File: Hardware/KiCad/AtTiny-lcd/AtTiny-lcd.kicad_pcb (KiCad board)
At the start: 2 copper layers, 7 parts, among them J1 Conn_01x04_Pin, J2 Conn_01x04_Pin, Q1 BC817, U1 ATtiny414-SS

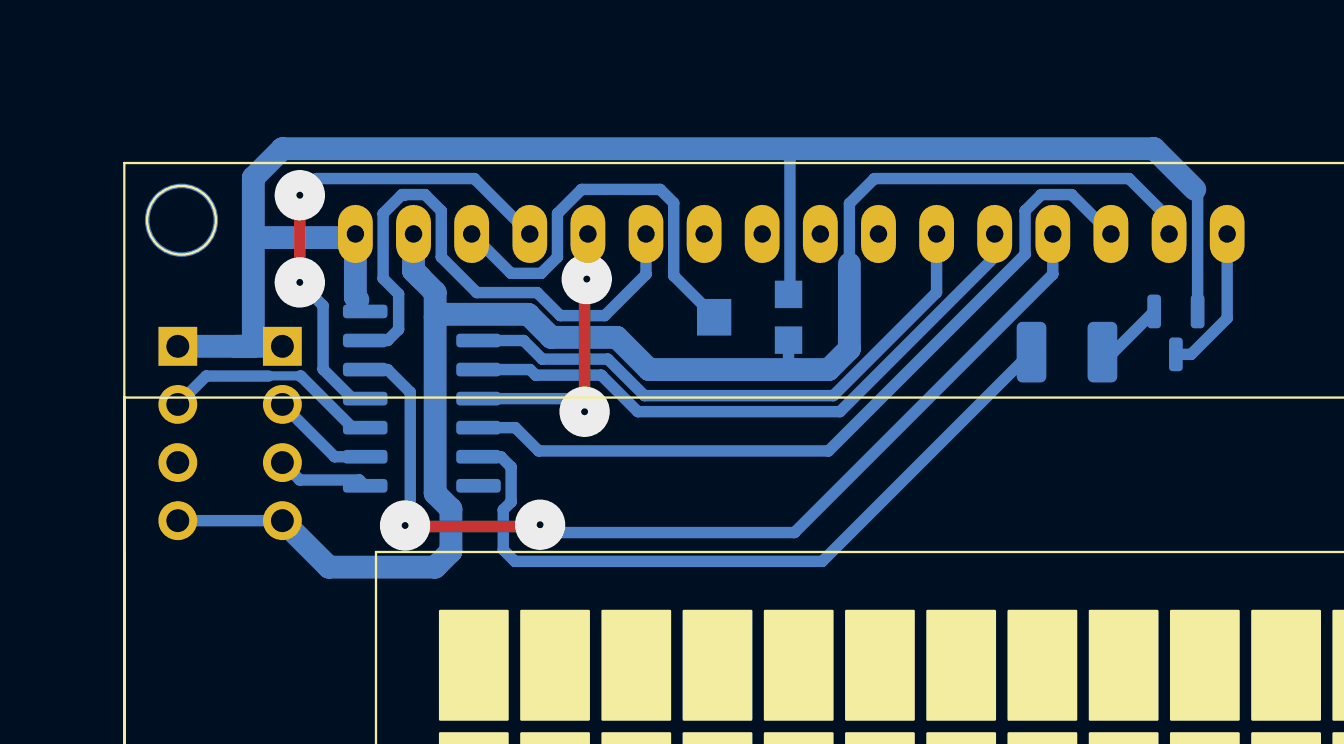
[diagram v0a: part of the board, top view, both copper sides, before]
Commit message: Backlight dimming
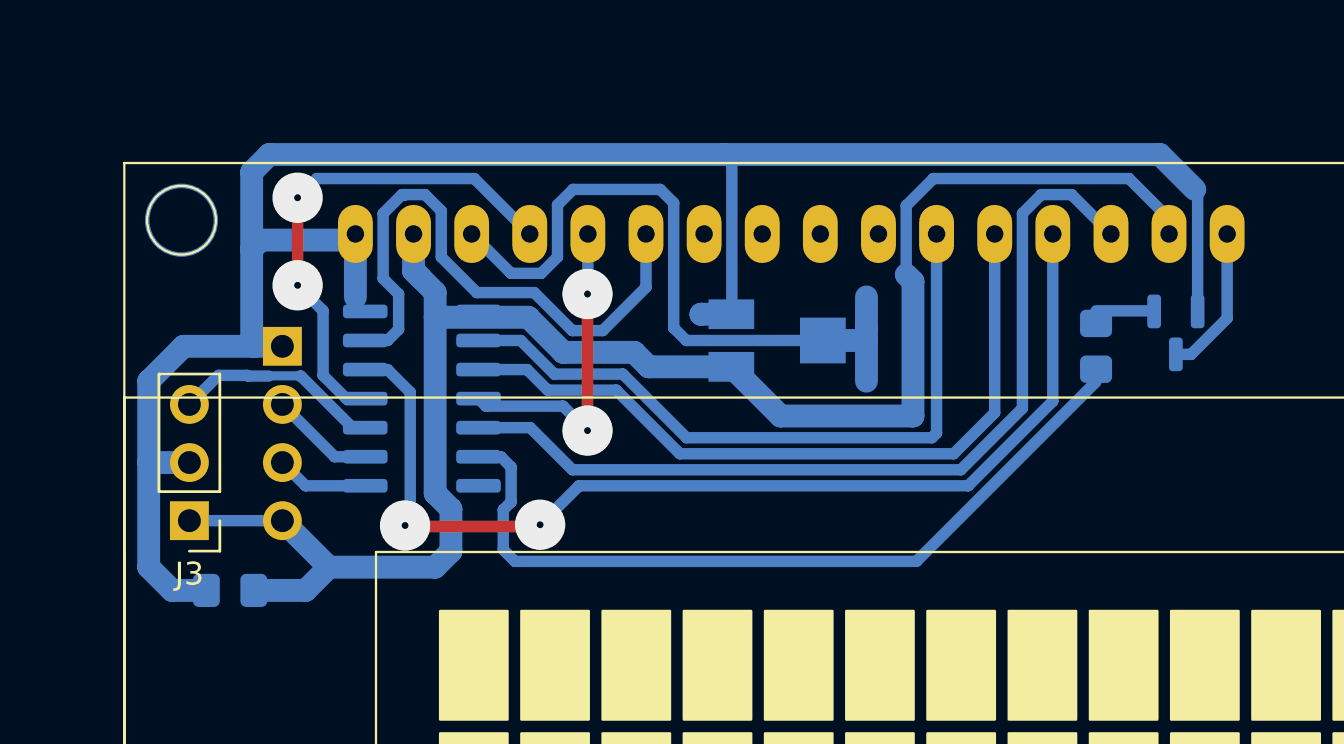
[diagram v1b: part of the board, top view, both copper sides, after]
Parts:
- removed J1: Conn_01x04_Pin, Connector_PinHeader_2.54mm:PinHeader_1x04_P2.54mm_Vertical
- added C1: 100n, Capacitor_SMD:C_0805_2012Metric_Pad1.18x1.45mm_HandSolder, B.Cu at (53.1, 47.8)
- added J3: Conn_01x03_Pin, Connector_PinHeader_2.54mm:PinHeader_1x03_P2.54mm_Vertical, F.Cu at (51.3, 44.7)
- R1: value R -> 1k; footprint Resistor_SMD:R_1210_3225Metric_Pad1.30x2.65mm_HandSolder -> Resistor_SMD:R_0805_2012Metric_Pad1.20x1.40mm_HandSolder
- RV1: footprint Potentiometer_SMD:Potentiometer_Bourns_TC33X_Vertical -> Potentiometer_SMD:Potentiometer_Vishay_TS53YJ_Vertical
- moved RV1 1.65 mm to (77.0, 36.8)
- moved R1 1.30 mm to (90.9, 37.1), turned to 90 degrees
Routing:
- net GND: track 73.8 -> 91.2 mm
- net Net-(U2-V0): track 18.2 -> 30.4 mm
- net Net-(U1-PA5): track 27.1 -> 32.6 mm
- net +5V: track 71.2 -> 76.6 mm
- net Net-(U1-PA4): track 25.4 -> 30.6 mm
- net Net-(U1-PA7): track 34.5 -> 39.1 mm
- net Net-(U1-PA2): track 43.2 -> 46.2 mm
- net Net-(U1-PB3): track 32.5 -> 34.7 mm
- net Net-(U1-PA6): track 12.7 -> 13.9 mm
- net Net-(U1-PA3): track 24.8 -> 25.6 mm

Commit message: PCB updated
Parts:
- RV1: footprint Potentiometer_SMD:Potentiometer_Vishay_TS53YJ_Vertical -> ownFootprints:Potentiometer_SMD_EBay_10k
- moved RV1 1.42 mm to (78.1, 37.7)
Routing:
- net +5V: track 76.6 -> 81.3 mm
- net Net-(U1-PA4): track 30.6 -> 34.5 mm
- net Net-(U1-PA7): track 39.1 -> 41.5 mm
- net Net-(U1-PA5): track 32.6 -> 34.9 mm
- net Net-(U2-V0): track 30.4 -> 29.1 mm
- net Net-(U1-PA2): track 46.2 -> 47.6 mm
- net Net-(U1-PB3): track 34.7 -> 35.9 mm
- net Net-(U1-PA6): track 13.9 -> 13.2 mm

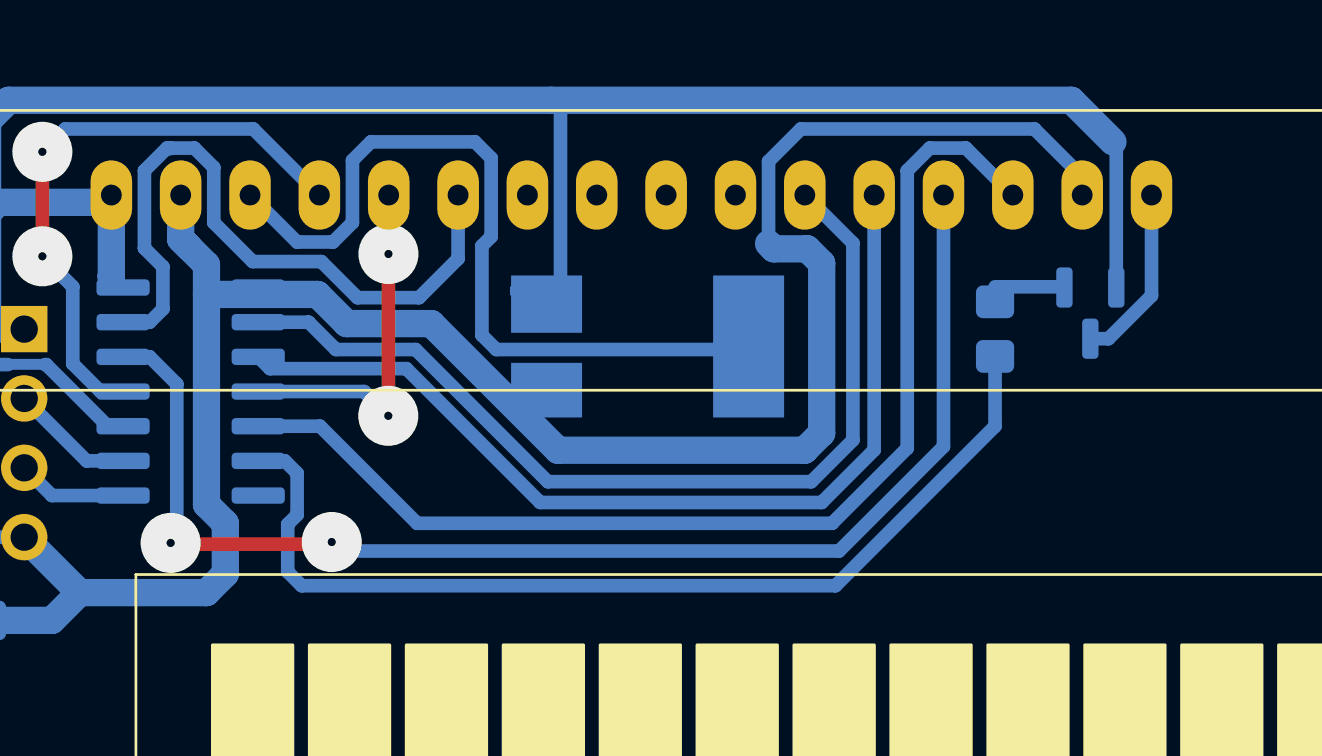
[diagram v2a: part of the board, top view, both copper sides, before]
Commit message: updated PCB dimming through ISR
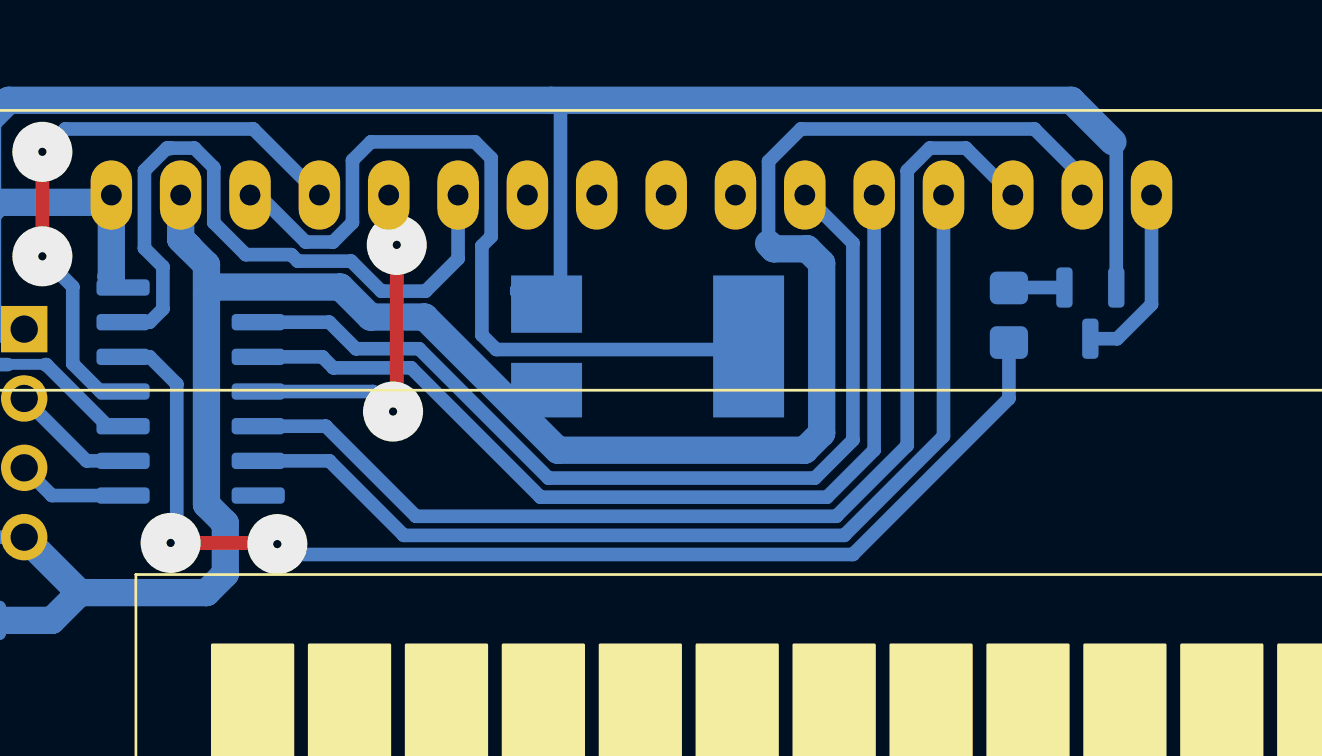
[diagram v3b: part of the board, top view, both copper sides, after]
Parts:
- moved R1 0.72 mm to (91.4, 36.6)
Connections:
- R1 pad 1: Net-(U1-PB3) -> Net-(U1-PA2)
- U2 pad 13: Net-(U1-PA2) -> Net-(U1-PB3)
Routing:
- net Net-(U1-PA2): track 47.6 -> 43.6 mm
- net Net-(U1-PB3): track 35.9 -> 36.6 mm
- net Net-(Q1-B): track 2.55 -> 2.04 mm

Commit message: update
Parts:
- U2: footprint ownFootprints:LCD2004 -> ownFootprints:LCD2008; moved to B.Cu
- moved U2 41.8 mm to (75.1, 61.3), turned to 90 degrees
- moved Q1 30.8 mm to (64.0, 32.1), turned to 0 degrees
- moved R1 30.7 mm to (61.1, 32.1)
- moved RV1 21.7 mm to (62.1, 52.3)
- moved C1 2.37 mm to (55.4, 48.4), turned to -90 degrees
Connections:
- RV1 pad 1: GND -> +5V
- RV1 pad 3: +5V -> GND
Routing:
- net Net-(U1-PA2): track 43.6 -> 6.43 mm, vias 2 -> 0
- net +5V: track 81.5 -> 51.5 mm
- net Net-(U1-PA5): track 34.7 -> 8.03 mm
- net Net-(U1-PA7): track 41.2 -> 15.4 mm, vias 0 -> 2
- net Net-(U1-PA4): track 34.4 -> 11.1 mm
- net GND: track 91.5 -> 107.0 mm
- net Net-(U2-V0): track 29.1 -> 13.9 mm
- net Net-(U1-PB3): track 36.6 -> 24.8 mm
- net Net-(U1-PA3): track 25.1 -> 32.6 mm, vias 0 -> 2
- net Net-(U1-PA6): track 13.4 -> 19.4 mm, vias 2 -> 0
- net Net-(U1-PA1): track 22.0 -> 20.0 mm
- net Net-(Q1-B): track 2.04 -> 2.75 mm
- net Net-(Q1-C): track 7.28 -> 6.71 mm
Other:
- board text added: "${REFERENCE}"
